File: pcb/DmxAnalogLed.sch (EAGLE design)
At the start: 37 parts, among them J1 RS485, J2 POWER_JACKPTH, J3 RS485, Q1 16MHz 10ppm, U1 ARDUINO_LEONARDO-REV3B_SMARTP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, U2 SN75176ASOIC, X1 USBPTH

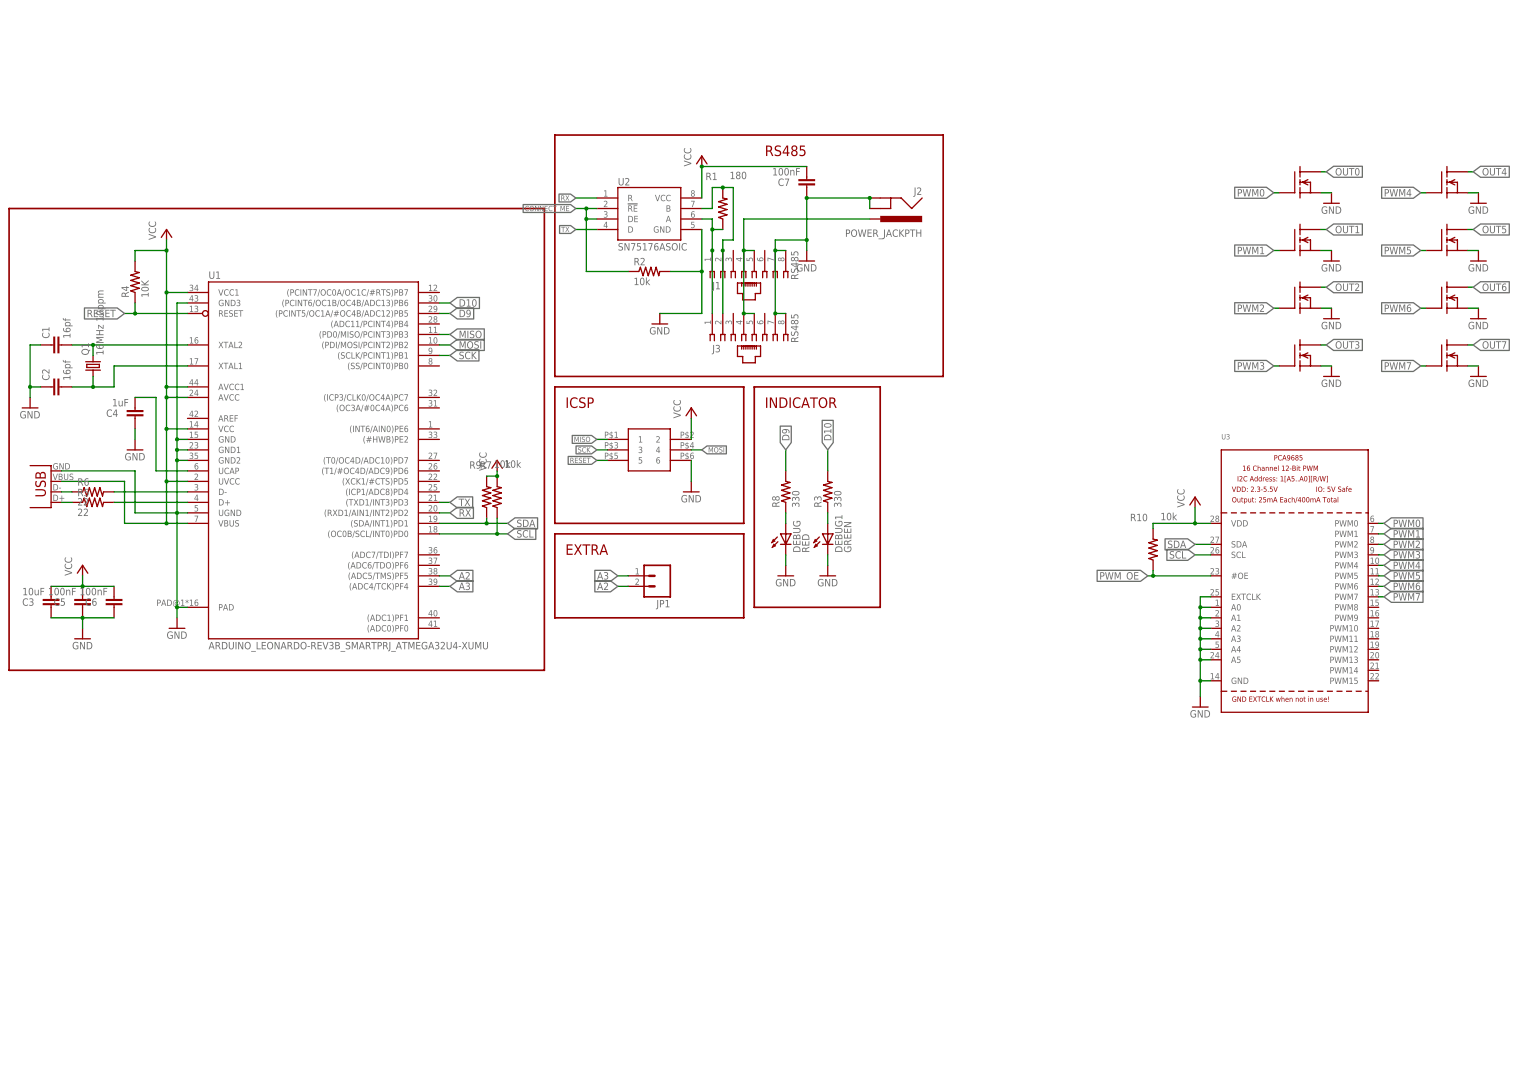
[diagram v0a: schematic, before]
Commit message: Add isolated RS485 circuit, begin transistor layout
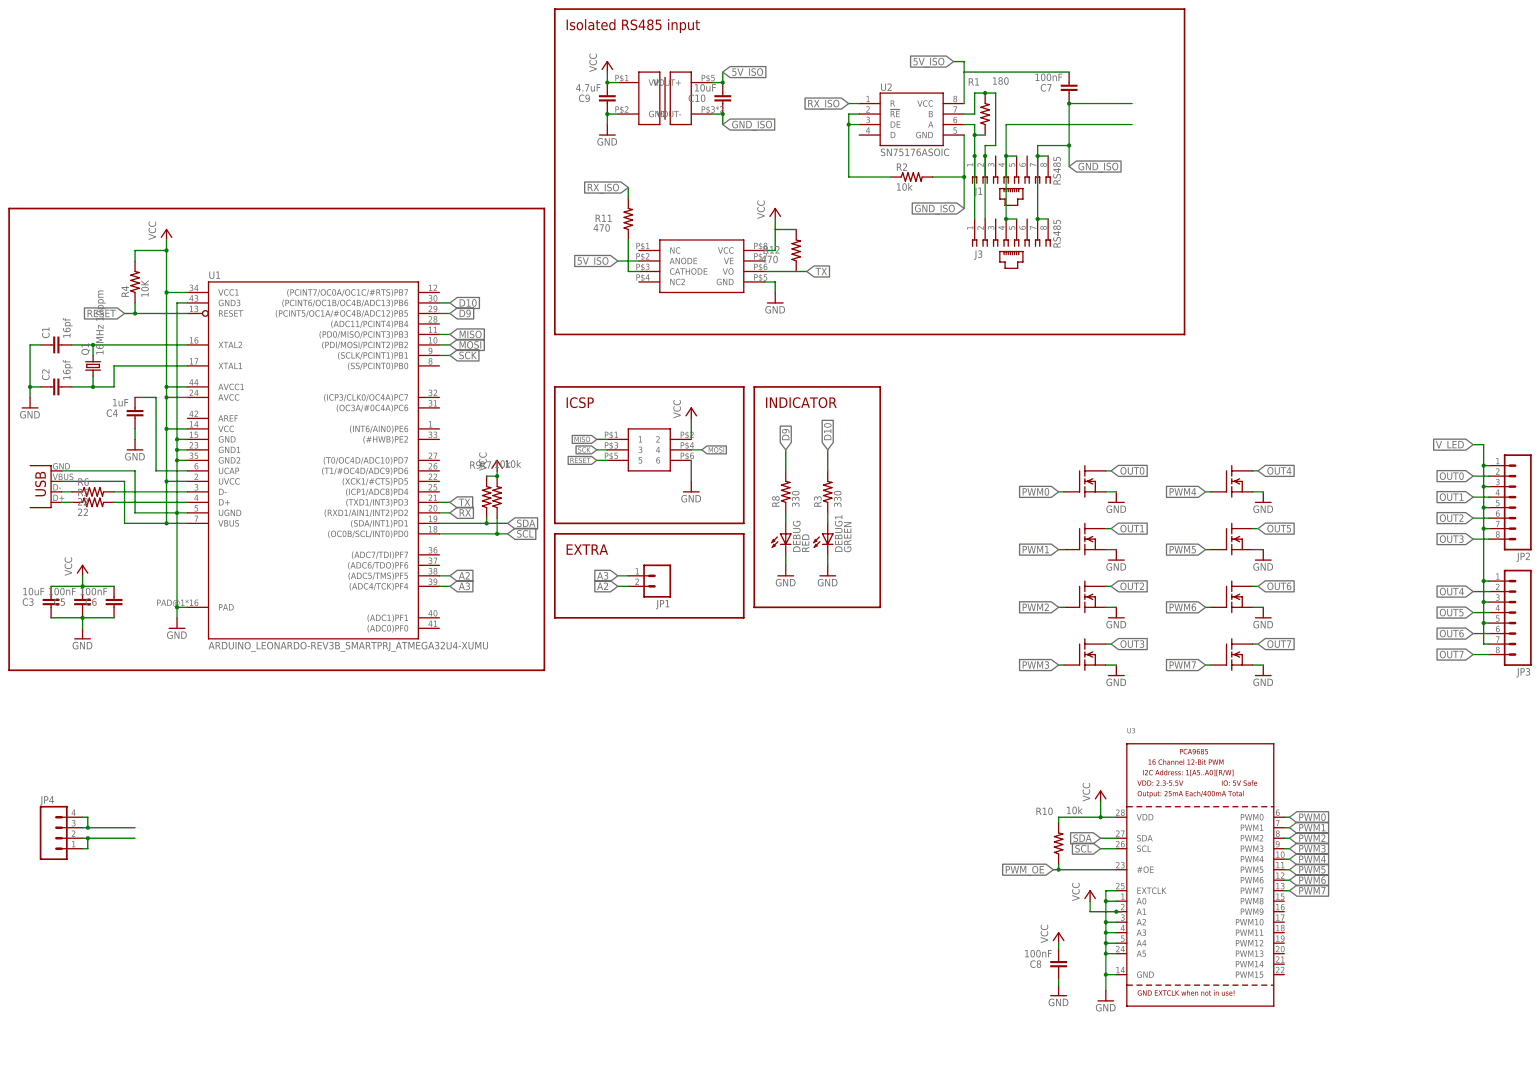
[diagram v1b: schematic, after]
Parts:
- removed J2: POWER_JACKPTH, SparkFun:POWER_JACKPTH
- added C10: 10uF, SparkFun:CAP0805
- added C8: 100nF, SparkFun:CAP0805
- added C9: 4.7uF, SparkFun:CAP0805
- added JP2, JP3: (no value), SparkFun:M083.5MM-8
- added JP4: (no value), SparkFun:M04SCREW
- added R11, R12: 470, SparkFun:RESISTOR
- added U$10: DC_DC_ISOLATED_0505, blinkiverse:DC_DC_ISOLATED_0505
- added U$12: 6N137, sonos_library:6N137
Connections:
- new net 5V_ISO: C10.2, C7.2, U$10.VOUT+, U$12.ANODE, U2.VCC
- new net GND_ISO: C10.1, C7.1, J1.7, J1.8, J3.7, J3.8, R2.2, U$10.VOUT-, U2.GND
- new net N$10: JP4.1, JP4.2
- new net N$13: JP4.3, JP4.4
- new net N$14: R11.1, U$12.CATHODE
- new net RX_ISO: R11.2, U2.R
- new net V_LED: JP2.1, JP2.3, JP2.5, JP2.7, JP3.1, JP3.3, JP3.5, JP3.7
- net GND: now also C8.1, C9.1, U$10.GND, U$12.GND; no longer C7.1, J1.7, J1.8, J2.GND, J2.GNDBREAK, J3.7, J3.8, R2.2, U2.GND, U3.A1
- net OUT0: now also JP2.2
- net OUT1: now also JP2.4
- net OUT2: now also JP2.6
- net OUT3: now also JP2.8
- net OUT4: now also JP3.2
- net OUT5: now also JP3.4
- net OUT6: now also JP3.6
- net OUT7: now also JP3.8
- net RX: no longer U2.R
- net TX: now also R12.1, U$12.VO; no longer U2.D
- net VCC: now also C8.2, C9.2, R12.2, U$10.VIN, U$12.VCC, U3.A1; no longer C7.2, U2.VCC
- net VMOT: no longer J2.PWR
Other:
- note added: "Isolated RS485 input"
- note removed: "RS485"
- moved on the sheet: C7, J1, J3, R1, R10, R2, U2, U3

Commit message: Remove PWM chip, start routing board
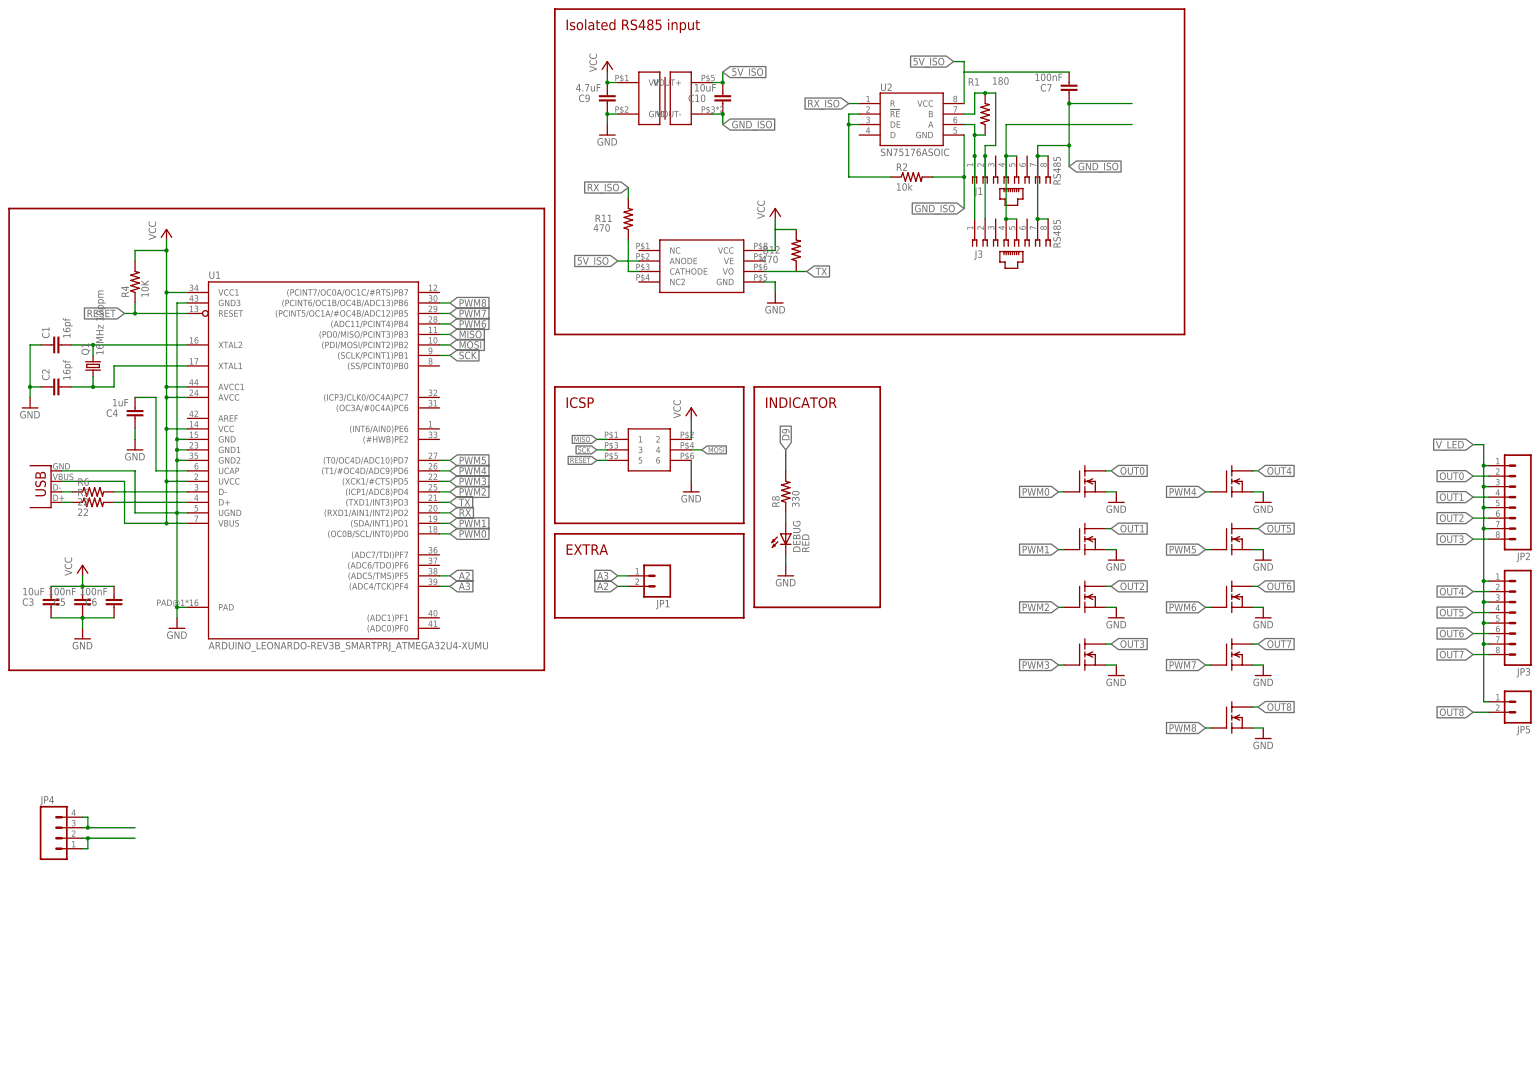
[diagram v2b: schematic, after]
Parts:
- removed C8: 100nF, SparkFun:CAP0805
- removed DEBUG1: GREEN, SparkFun:LED0805
- removed R10, R7, R9: 10k, SparkFun:RESISTOR
- removed R3: 330, SparkFun:RESISTOR
- removed U3: (no value), adafruit:PCA9685
- added JP5: (no value), SparkFun:M023.5MM
- added U$11: N_MOSFET, blinkiverse:N_MOSFET
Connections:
- removed net D10: R3.2, U1.(PCINT6/OC1B/OC4B/ADC13)PB6
- removed net N$7: DEBUG1.A, R3.1
- removed net PWM_OE: R10.1, U3.#OE
- removed net SCL: R7.1, U1.(OC0B/SCL/INT0)PD0, U3.SCL
- removed net SDA: R9.1, U1.(SDA/INT1)PD1, U3.SDA
- new net OUT8: JP5.2, U$11.D
- new net PWM8: U$11.G, U1.(PCINT6/OC1B/OC4B/ADC13)PB6
- net D9: no longer U1.(PCINT5/OC1A/#OC4B/ADC12)PB5
- net GND: now also U$11.S; no longer C8.1, DEBUG1.C, U3.A0, U3.A2, U3.A3, U3.A4, U3.A5, U3.EXTCLK, U3.GND
- net PWM0: now also U1.(OC0B/SCL/INT0)PD0; no longer U3.PWM0
- net PWM1: now also U1.(SDA/INT1)PD1; no longer U3.PWM1
- net PWM2: now also U1.(ICP1/ADC8)PD4; no longer U3.PWM2
- net PWM3: now also U1.(XCK1/#CTS)PD5; no longer U3.PWM3
- net PWM4: now also U1.(T1/#OC4D/ADC9)PD6; no longer U3.PWM4
- net PWM5: now also U1.(T0/OC4D/ADC10)PD7; no longer U3.PWM5
- net PWM6: now also U1.(ADC11/PCINT4)PB4; no longer U3.PWM6
- net PWM7: now also U1.(PCINT5/OC1A/#OC4B/ADC12)PB5; no longer U3.PWM7
- net VCC: no longer C8.2, R10.2, R7.2, R9.2, U3.A1, U3.VDD
- net V_LED: now also JP5.1

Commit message: Start laying out board
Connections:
- removed net N$10: JP4.1, JP4.2
- removed net N$13: JP4.3, JP4.4
- net GND: now also JP4.3, JP4.4
- net PWM2: now also U1.(XCK1/#CTS)PD5; no longer U1.(ICP1/ADC8)PD4
- net PWM3: now also U1.(ICP1/ADC8)PD4; no longer U1.(XCK1/#CTS)PD5
- net V_LED: now also JP4.1, JP4.2
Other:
- moved on the sheet: JP4
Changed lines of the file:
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@@
 <part name="GND8" library="supply1" deviceset="GND" device=""/>
 <part name="JP5" library="SparkFun" deviceset="M02" device="3.5MM"/>
+<part name="GND3" library="supply1" deviceset="GND" device=""/>
 </parts>
 <sheets>
@@
 <instance part="JP2" gate="G$1" x="332.74" y="8.89" rot="R180"/>
 <instance part="JP3" gate="G$1" x="332.74" y="-19.05" rot="R180"/>
-<instance part="JP4" gate="G$1" x="-17.78" y="-73.66"/>
+<instance part="JP4" gate="G$1" x="-19.05" y="-71.12" rot="MR180"/>
 <instance part="U$10" gate="G$1" x="127" y="104.14"/>
 <instance part="P+8" gate="VCC" x="114.3" y="114.3"/>
@@
 <instance part="GND8" gate="1" x="273.05" y="-49.53"/>
 <instance part="JP5" gate="G$1" x="335.28" y="-40.64" rot="R180"/>
+<instance part="GND3" gate="1" x="-2.54" y="-83.82"/>
 </instances>
 <busses>
@@
 <wire x1="270.51" y1="-46.99" x2="273.05" y2="-46.99" width="0.1524" layer="91"/>
 <pinref part="GND8" gate="1" pin="GND"/>
+</segment>
+<segment>
+<wire x1="-11.43" y1="-76.2" x2="-11.43" y2="-73.66" width="0.1524" layer="91"/>
+<wire x1="-11.43" y1="-76.2" x2="-2.54" y2="-76.2" width="0.1524" layer="91"/>
+<wire x1="-2.54" y1="-76.2" x2="-2.54" y2="-81.28" width="0.1524" layer="91"/>
+<pinref part="GND3" gate="1" pin="GND"/>
+<pinref part="JP4" gate="G$1" pin="3"/>
+<wire x1="-13.97" y1="-73.66" x2="-11.43" y2="-73.66" width="0.1524" layer="91"/>
+<pinref part="JP4" gate="G$1" pin="4"/>
+<wire x1="-11.43" y1="-76.2" x2="-13.97" y2="-76.2" width="0.1524" layer="91"/>
+<junction x="-11.43" y="-76.2"/>
 </segment>
 </net>
@@
 </segment>
 <segment>
+<pinref part="U1" gate="G$1" pin="(XCK1/#CTS)PD5"/>
+<wire x1="73.66" y1="12.7" x2="76.2" y2="12.7" width="0.1524" layer="91"/>
+<label x="76.2" y="12.7" size="1.778" layer="95" xref="yes"/>
+</segment>
+</net>
+<net name="PWM3" class="0">
+<segment>
+<pinref part="U$5" gate="G$1" pin="G"/>
+<wire x1="224.79" y1="-31.75" x2="223.52" y2="-31.75" width="0.1524" layer="91"/>
+<label x="223.52" y="-31.75" size="1.778" layer="95" rot="R180" xref="yes"/>
+</segment>
+<segment>
 <pinref part="U1" gate="G$1" pin="(ICP1/ADC8)PD4"/>
 <wire x1="73.66" y1="10.16" x2="76.2" y2="10.16" width="0.1524" layer="91"/>
 <label x="76.2" y="10.16" size="1.778" layer="95" xref="yes"/>
-</segment>
-</net>
-<net name="PWM3" class="0">
-<segment>
-<pinref part="U$5" gate="G$1" pin="G"/>
-<wire x1="224.79" y1="-31.75" x2="223.52" y2="-31.75" width="0.1524" layer="91"/>
-<label x="223.52" y="-31.75" size="1.778" layer="95" rot="R180" xref="yes"/>
-</segment>
-<segment>
-<pinref part="U1" gate="G$1" pin="(XCK1/#CTS)PD5"/>
-<wire x1="73.66" y1="12.7" x2="76.2" y2="12.7" width="0.1524" layer="91"/>
-<label x="76.2" y="12.7" size="1.778" layer="95" xref="yes"/>
 </segment>
 </net>
@@
 <junction x="326.39" y="-26.67"/>
 </segment>
-</net>
-<net name="N$10" class="0">
-<segment>
+<segment>
+<wire x1="-11.43" y1="-68.58" x2="-2.54" y2="-68.58" width="0.1524" layer="91"/>
+<wire x1="-2.54" y1="-68.58" x2="-2.54" y2="-66.04" width="0.1524" layer="91"/>
+<wire x1="-11.43" y1="-68.58" x2="-11.43" y2="-71.12" width="0.1524" layer="91"/>
+<label x="-2.54" y="-66.04" size="1.778" layer="95" rot="R90" xref="yes"/>
 <pinref part="JP4" gate="G$1" pin="2"/>
-<wire x1="-12.7" y1="-73.66" x2="-11.43" y2="-73.66" width="0.1524" layer="91"/>
+<wire x1="-13.97" y1="-71.12" x2="-11.43" y2="-71.12" width="0.1524" layer="91"/>
 <pinref part="JP4" gate="G$1" pin="1"/>
-<wire x1="-12.7" y1="-76.2" x2="-11.43" y2="-76.2" width="0.1524" layer="91"/>
-<wire x1="-11.43" y1="-76.2" x2="-11.43" y2="-73.66" width="0.1524" layer="91"/>
-<wire x1="-11.43" y1="-73.66" x2="0" y2="-73.66" width="0.1524" layer="91"/>
-<junction x="-11.43" y="-73.66"/>
-</segment>
-</net>
-<net name="N$13" class="0">
-<segment>
-<pinref part="JP4" gate="G$1" pin="3"/>
-<wire x1="-12.7" y1="-71.12" x2="-11.43" y2="-71.12" width="0.1524" layer="91"/>
-<pinref part="JP4" gate="G$1" pin="4"/>
-<wire x1="-11.43" y1="-71.12" x2="0" y2="-71.12" width="0.1524" layer="91"/>
-<wire x1="-12.7" y1="-68.58" x2="-11.43" y2="-68.58" width="0.1524" layer="91"/>
-<wire x1="-11.43" y1="-68.58" x2="-11.43" y2="-71.12" width="0.1524" layer="91"/>
-<junction x="-11.43" y="-71.12"/>
-</segment>
-</net>
+<wire x1="-11.43" y1="-68.58" x2="-13.97" y2="-68.58" width="0.1524" layer="91"/>
+<junction x="-11.43" y="-68.58"/>
+</segment>
+</net>

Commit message: Routed, pending review
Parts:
- removed DEBUG: RED, SparkFun:LED0805
- removed JP1: (no value), SparkFun:M02PTH
- added C11: .3uF, SparkFun:CAP0805
- added C12: .1uF, SparkFun:CAP0805
- added C13: .3uF, SparkFun:CAP1210
- added C14: .1uF, SparkFun:CAP1210
- added C15: ?uF, SparkFun:CAP0805
- added C16: 4.7uF, SparkFun:CAP1210
- added C17: 10uF, SparkFun:CAP1210
- added C18, C19, C20, C21: ?uF, SparkFun:CAP1210
- added C8: 1uF, SparkFun:CAP0805
- added IC2: 7805TV, linear:7805TV
- added J2: POWER_JACKPTH, SparkFun:POWER_JACKPTH
- added JP6: (no value), SparkFun:M05PTH
- added LED1: (no value), SparkFun:LED5MM
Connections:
- removed net D9: R8.2
- removed net V_LED: JP2.1, JP2.3, JP2.5, JP2.7, JP3.1, JP3.3, JP3.5, JP3.7, JP4.1, JP4.2, JP5.1
- new net A1: JP6.2, U1.(ADC6/TDO)PF6
- new net LED: R8.2, U1.(OC3A/#0C4A)PC6
- new net N$10: C8.2, U1.VBUS, X1.VBUS
- new net N$11: C15.2, U1.AREF
- new net V_PWM: C11.2, C13.1, C18.1, C19.1, C20.1, C21.1, IC2.VI, J2.PWR, JP2.1, JP2.3, JP2.5, JP2.7, JP3.1, JP3.3, JP3.5, JP3.7, JP4.1, JP4.2, JP5.1
- net 5V_ISO: now also C17.1
- net A2: now also JP6.3; no longer JP1.2
- net A3: now also JP6.4; no longer JP1.1
- net GND: now also C11.1, C12.1, C13.2, C14.2, C15.1, C16.2, C18.2, C19.2, C20.2, C21.2, C8.1, IC2.GND, J2.GND, J2.GNDBREAK, JP6.5, LED1.C; no longer DEBUG.C
- net GND_ISO: now also C17.2
- net N$8: now also LED1.A; no longer DEBUG.A
- net VCC: now also C12.2, C14.1, C16.1, IC2.VO, JP6.1; no longer U1.VBUS, X1.VBUS
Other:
- note added: "POWER"
- note added: "PWM"
- note added: "THINK"
- moved on the sheet: C10, C3, C4, C5, C6, C7, C9, J1, J3, JP2, JP3, JP4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
